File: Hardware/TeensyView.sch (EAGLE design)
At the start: 9 parts

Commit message: Proto 1 design complete
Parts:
- removed J3: (no value), SparkFun-Connectors:CONN_01
- added C1, C2, C3, C4: 1.0uF, SparkFun-Capacitors:1.0UF-0402-16V-10%
- added C5: 2.2uF, SparkFun-Capacitors:2.2UF-0805-25V-(+80/-20%)
- added C6: 4.7UF, SparkFun-Capacitors:4.7UF-1206-16V-(+80/-20%)
- added JP1, JP2, JP3: JUMPER-SMT_3_1-NC_TRACE_SILK, SparkFun-Jumpers:JUMPER-SMT_3_1-NC_TRACE_SILK
- added OLED1: OLED128X64SIDEREAR-MOUNT, TeensyViewDev:OLED128X64SIDEREAR-MOUNT
- added R1: 330k, SparkFun-Resistors:330KOHM-0603-1/10W-1%
- J1, J2: value (none) -> DNP; device SparkFun-Connectors:CONN_14 -> SparkFun-Connectors:CONN_14NO_SILK
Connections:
- new net !CS: JP1.2, OLED1.!CS!
- new net !RESET: J1.8, OLED1.!RESET!
- new net D/!C: J1.7, OLED1.D/!C!
- new net N$1: J1.12, JP1.3
- new net N$10: J2.1, JP3.3
- new net N$11: J2.7, JP3.1
- new net N$12: J1.13, JP2.3
- new net N$13: J2.6, JP2.1
- new net N$2: J1.11, JP1.1
- new net N$3: C4.2, OLED1.C1N
- new net N$4: C4.1, OLED1.C1P
- new net N$5: C3.2, OLED1.C2N
- new net N$6: C3.1, OLED1.C2P
- new net N$7: OLED1.IREF, R1.2
- new net N$8: C6.1, OLED1.VCOMH
- new net N$9: C5.1, OLED1.VCC
- new net SCLK: JP3.2, OLED1.SCLK
- new net SDIN: JP2.2, OLED1.SDIN
- new net VCC: C1.1, C2.1, J2.12, OLED1.VDD, OLED1.VDDB
- net GND: now also C1.2, C2.2, C5.2, C6.2, J1.1, OLED1.VSS, R1.1; no longer J3.1
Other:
- note added: "10"
- note added: "11"
- note added: "128x32 OLED on the Teensy 3 footprint."
- note added: "13"
- note added: "9"
- note added: "A4"
- note added: "A5"
- note added: "Connect directly to Teensy. Draws 30mA from the Teensy's 3.3v regulator."
- note added: "Teensy pin 0"
- note added: "Teensy pin 12"
- note added: "Teensy pin 13"
- note added: "Teensy pin 23"
- note added: "TeensyView"
- note added: "To use SPI: JP1: Select Chip Select. Choose (10 default) or 9. JP2: Select MOSI on pin 11 (default). JP3: Select SCLK on pin 13 (default). To use I2C: JP1: Drive logic high on pin 10 or 9. JP2: Select SDA0 on pin A4 JP3: Select SCL0 on pin A5"
- moved on the sheet: J1, J2

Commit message: Post review fixes
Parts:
- added JP4: JUMPER-SMT_3_2-NC_TRACE_SILK, SparkFun-Jumpers:JUMPER-SMT_3_2-NC_TRACE_SILK
- added R2, R3, R4: 4.7k, SparkFun-Resistors:4.7KOHM-0603-1/10W-1%
- C6: PROD_ID (none) -> CAP-10300
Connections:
- new net A4PU: JP4.3, R2.2
- new net A5PU: JP4.1, R3.2
- net !CS: now also R4.1
- net N$11: now also R3.1
- net N$13: now also R2.1
- net VCC: now also JP4.2, R4.2
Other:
- note added: "OLED Connections"
- note added: "Teensy Connections"
- note added: "To use SPI: JP1: Select Chip Select. Choose (10 default) or 9. JP2: Select MOSI on pin 11 (default). JP3: Select SCLK on pin 13 (default). To use I2C (Address: 0x7A): JP1: Drive logic high on pin 10 or 9. JP2: Select SDA0 on pin A4 JP3: Select SCL0 on pin A5"
- note removed: "To use SPI: JP1: Select Chip Select. Choose (10 default) or 9. JP2: Select MOSI on pin 11 (default). JP3: Select SCLK on pin 13 (default). To use I2C: JP1: Drive logic high on pin 10 or 9. JP2: Select SDA0 on pin A4 JP3: Select SCL0 on pin A5"
- moved on the sheet: J1, J2, JP1, JP2, JP3

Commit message: Going for proto 2
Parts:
- removed R2, R3: 4.7k, SparkFun-Resistors:4.7KOHM-0603-1/10W-1%
- added JP5: JUMPER-SMT_3_1-NC_TRACE_SILK, SparkFun-Jumpers:JUMPER-SMT_3_1-NC_TRACE_SILK
- JP4: value JUMPER-SMT_3_2-NC_TRACE_SILK -> JUMPER-SMT_3_1-NC_TRACE_SILK; device SparkFun-Jumpers:JUMPER-SMT_3_2-NC_TRACE_SILK -> SparkFun-Jumpers:JUMPER-SMT_3_1-NC_TRACE_SILK
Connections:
- removed net A4PU: JP4.3, R2.2
- removed net A5PU: JP4.1, R3.2
- new net N$14: J2.3, JP4.3
- new net N$15: J1.4, JP4.1
- new net N$16: J1.7, JP5.3
- new net N$17: J2.9, JP5.1
- net !RESET: now also JP4.2; no longer J1.8
- net D/!C: now also JP5.2; no longer J1.7
- net N$11: now also J2.2; no longer J2.7, R3.1
- net N$13: now also J1.9; no longer J2.6, R2.1
- net N$2: now also J2.8; no longer J1.11
- net VCC: no longer JP4.2
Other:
- note added: "14"
- note added: "15"
- note added: "2"
- note added: "20"
- note added: "21"
- note added: "5"
- note added: "7"
- note added: "Alternate( Audio Shield Compatible) D/!C!: 21 CS: 20 MOSI: 7 SCLK: 14 !RESET!: 2"
- note added: "Always connect power and ground as well."
- note added: "Connect directly to Teensy. Draws <1mA from the Teensy's 3.3v regulator. (1.6V to 4.0V tolerant)"
- note added: "Default (copper link side): D/!C!: 5 CS: 10 MOSI: 11 SCLK: 13 !RESET!: 15"
- note added: "User jumpers 1-5 to configure where the OLED's control lines are connected, then configure with code to match."
- note added: "v02"
- note removed: "9"
- note removed: "A5"
- note removed: "Connect directly to Teensy. Draws 30mA from the Teensy's 3.3v regulator."
- note removed: "To use SPI: JP1: Select Chip Select. Choose (10 default) or 9. JP2: Select MOSI on pin 11 (default). JP3: Select SCLK on pin 13 (default). To use I2C (Address: 0x7A): JP1: Drive logic high on pin 10 or 9. JP2: Select SDA0 on pin A4 JP3: Select SCL0 on pin A5"
- note removed: "v01"
- moved on the sheet: J1, J2, JP1, JP2, JP3, R4

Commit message: Moved silk.
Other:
- note added: "Connect directly to Teensy. Draws ~16mA from the Teensy's 3.3v regulator. (1.6V to 4.0V tolerant)"
- note removed: "Connect directly to Teensy. Draws <1mA from the Teensy's 3.3v regulator. (1.6V to 4.0V tolerant)"
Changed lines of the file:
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@@
 </text>
 <text x="5.08" y="175.26" size="5.08" layer="97" font="vector">TeensyView</text>
-<text x="10.16" y="167.64" size="1.778" layer="97" font="vector" align="top-left">Connect directly to Teensy.  Draws &lt;1mA from the
+<text x="10.16" y="167.64" size="1.778" layer="97" font="vector" align="top-left">Connect directly to Teensy.  Draws ~16mA from the
 Teensy's 3.3v regulator.
 (1.6V to 4.0V tolerant)</text>

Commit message: Applied Proto 2 review action items
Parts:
- R1: value 330k -> 820k; device SparkFun-Resistors:330KOHM-0603-1/10W-1% -> SparkFun-Resistors:820KOHM-0603-1/10W-1%
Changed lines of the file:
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@@
 <attribute name="PROD_ID" value="CAP-10300"/>
 </part>
-<part name="R1" library="SparkFun-Resistors" deviceset="330KOHM" device="-0603-1/10W-1%" value="330k"/>
+<part name="R1" library="SparkFun-Resistors" deviceset="820KOHM" device="-0603-1/10W-1%" value="820k"/>
 <part name="GND4" library="SparkFun-PowerSymbols" deviceset="GND" device=""/>
 <part name="GND5" library="SparkFun-PowerSymbols" deviceset="GND" device=""/>

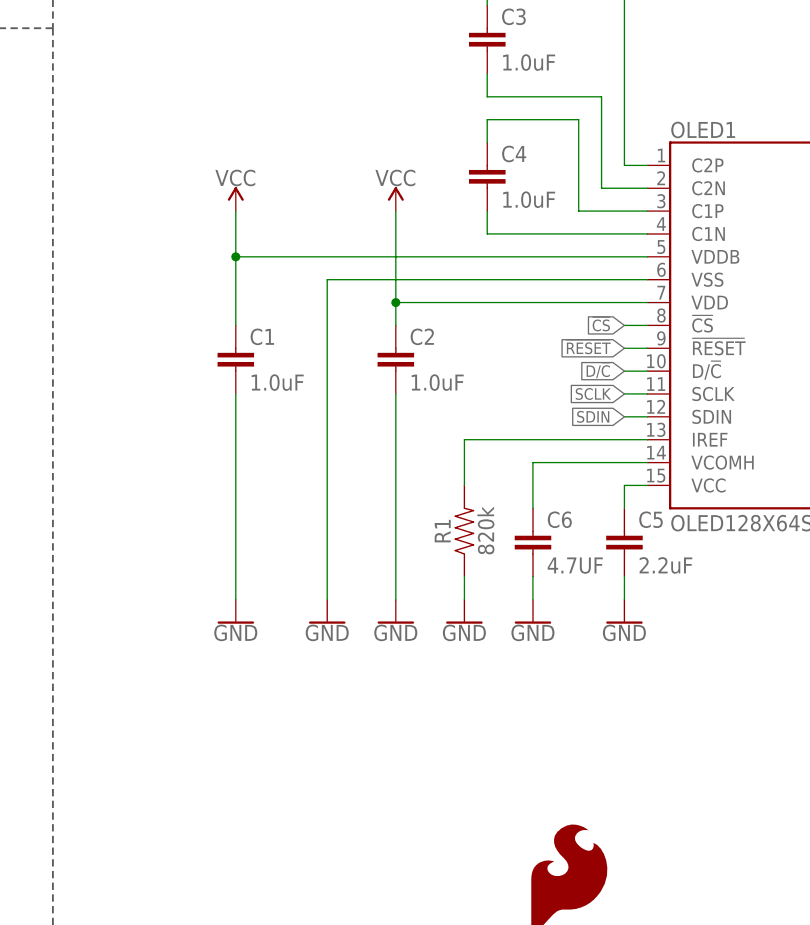
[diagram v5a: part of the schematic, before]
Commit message: Added TP to OLED's VCC
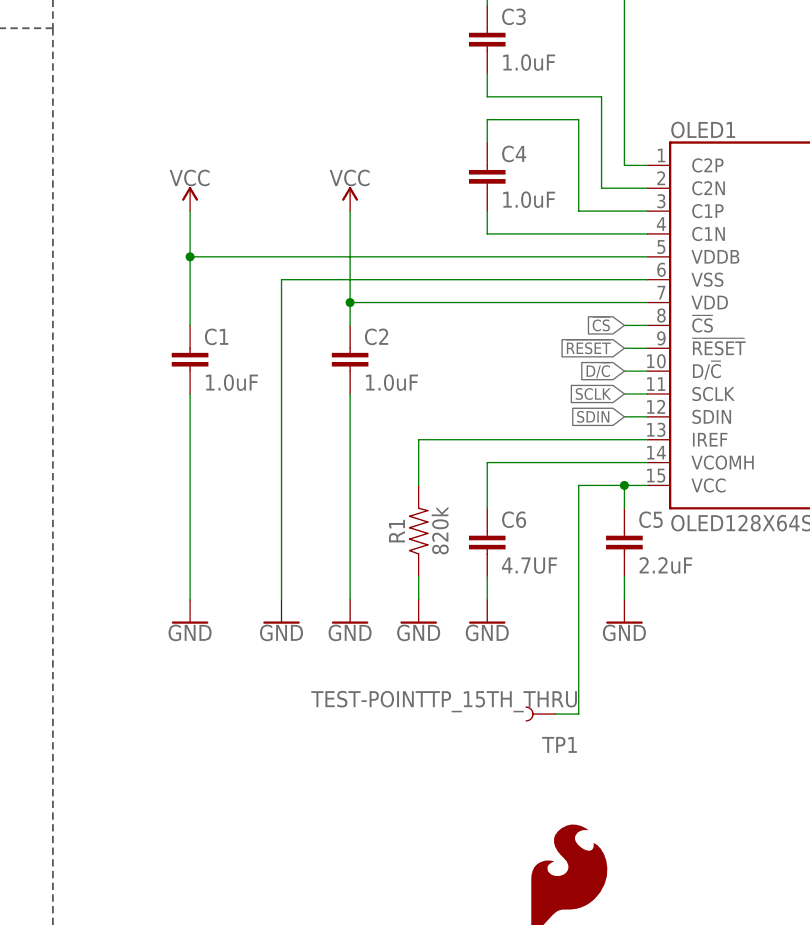
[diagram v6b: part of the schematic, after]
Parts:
- added TP1: TEST-POINTTP_15TH_THRU, SparkFun-Connectors:TEST-POINTTP_15TH_THRU
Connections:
- net N$9: now also TP1.1
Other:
- moved on the sheet: C1, C2, C6, R1
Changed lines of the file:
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@@
 <part name="JP4" library="SparkFun-Jumpers" deviceset="JUMPER-SMT_3_1-NC_TRACE" device="_SILK" value="JUMPER-SMT_3_1-NC_TRACE_SILK"/>
 <part name="JP5" library="SparkFun-Jumpers" deviceset="JUMPER-SMT_3_1-NC_TRACE" device="_SILK" value="JUMPER-SMT_3_1-NC_TRACE_SILK"/>
+<part name="TP1" library="SparkFun-Connectors" deviceset="TEST-POINT" device="TP_15TH_THRU" value="TEST-POINTTP_15TH_THRU"/>
 </parts>
 <sheets>
@@
 <instance part="LOGO3" gate="G$1" x="152.4" y="40.64"/>
 <instance part="OLED1" gate="G$1" x="213.36" y="121.92"/>
-<instance part="C1" gate="G$1" x="152.4" y="116.84"/>
-<instance part="C2" gate="G$1" x="170.18" y="116.84"/>
-<instance part="GND2" gate="1" x="170.18" y="88.9"/>
-<instance part="GND3" gate="1" x="152.4" y="88.9"/>
+<instance part="C1" gate="G$1" x="147.32" y="116.84"/>
+<instance part="C2" gate="G$1" x="165.1" y="116.84"/>
+<instance part="GND2" gate="1" x="165.1" y="88.9"/>
+<instance part="GND3" gate="1" x="147.32" y="88.9"/>
 <instance part="C3" gate="G$1" x="180.34" y="152.4"/>
 <instance part="C4" gate="G$1" x="180.34" y="137.16"/>
 <instance part="C5" gate="G$1" x="195.58" y="96.52"/>
-<instance part="C6" gate="G$1" x="185.42" y="96.52">
-<attribute name="PROD_ID" x="185.42" y="96.52" size="1.27" layer="96" display="off"/>
-</instance>
-<instance part="R1" gate="G$1" x="177.8" y="99.06" rot="R90"/>
+<instance part="C6" gate="G$1" x="180.34" y="96.52">
+<attribute name="PROD_ID" x="180.34" y="96.52" size="1.27" layer="96" display="off"/>
+</instance>
+<instance part="R1" gate="G$1" x="172.72" y="99.06" rot="R90"/>
 <instance part="GND4" gate="1" x="195.58" y="88.9"/>
-<instance part="GND5" gate="1" x="185.42" y="88.9"/>
-<instance part="GND6" gate="1" x="177.8" y="88.9"/>
-<instance part="GND7" gate="1" x="162.56" y="88.9"/>
+<instance part="GND5" gate="1" x="180.34" y="88.9"/>
+<instance part="GND6" gate="1" x="172.72" y="88.9"/>
+<instance part="GND7" gate="1" x="157.48" y="88.9"/>
 <instance part="GND8" gate="1" x="27.94" y="78.74" rot="MR0"/>
-<instance part="SUPPLY1" gate="G$1" x="152.4" y="134.62"/>
-<instance part="SUPPLY2" gate="G$1" x="170.18" y="134.62"/>
+<instance part="SUPPLY1" gate="G$1" x="147.32" y="134.62"/>
+<instance part="SUPPLY2" gate="G$1" x="165.1" y="134.62"/>
 <instance part="SUPPLY3" gate="G$1" x="106.68" y="91.44"/>
 <instance part="JP1" gate="G$1" x="78.74" y="63.5" smashed="yes" rot="MR90">
@@
 <attribute name="NAME" x="58.42" y="70.739" size="1.778" layer="95" font="vector" rot="MR180" align="top-left"/>
 </instance>
+<instance part="TP1" gate="G$1" x="187.96" y="78.74" rot="R180"/>
 </instances>
 <busses>
@@
 <pinref part="C2" gate="G$1" pin="2"/>
 <pinref part="GND2" gate="1" pin="GND"/>
-<wire x1="170.18" y1="114.3" x2="170.18" y2="91.44" width="0.1524" layer="91"/>
+<wire x1="165.1" y1="114.3" x2="165.1" y2="91.44" width="0.1524" layer="91"/>
 </segment>
 <segment>
 <pinref part="GND3" gate="1" pin="GND"/>
 <pinref part="C1" gate="G$1" pin="2"/>
-<wire x1="152.4" y1="91.44" x2="152.4" y2="114.3" width="0.1524" layer="91"/>
+<wire x1="147.32" y1="91.44" x2="147.32" y2="114.3" width="0.1524" layer="91"/>
 </segment>
 <segment>
@@
 <pinref part="GND5" gate="1" pin="GND"/>
 <pinref part="C6" gate="G$1" pin="2"/>
-<wire x1="185.42" y1="93.98" x2="185.42" y2="91.44" width="0.1524" layer="91"/>
+<wire x1="180.34" y1="93.98" x2="180.34" y2="91.44" width="0.1524" layer="91"/>
 </segment>
 <segment>
 <pinref part="GND6" gate="1" pin="GND"/>
 <pinref part="R1" gate="G$1" pin="1"/>
-<wire x1="177.8" y1="91.44" x2="177.8" y2="93.98" width="0.1524" layer="91"/>
+<wire x1="172.72" y1="91.44" x2="172.72" y2="93.98" width="0.1524" layer="91"/>
 </segment>
 <segment>
 <pinref part="OLED1" gate="G$1" pin="VSS"/>
 <pinref part="GND7" gate="1" pin="GND"/>
-<wire x1="198.12" y1="127" x2="162.56" y2="127" width="0.1524" layer="91"/>
-<wire x1="162.56" y1="127" x2="162.56" y2="91.44" width="0.1524" layer="91"/>
+<wire x1="198.12" y1="127" x2="157.48" y2="127" width="0.1524" layer="91"/>
+<wire x1="157.48" y1="127" x2="157.48" y2="91.44" width="0.1524" layer="91"/>
 </segment>
 <segment>
@@
 <pinref part="OLED1" gate="G$1" pin="IREF"/>
 <pinref part="R1" gate="G$1" pin="2"/>
-<wire x1="198.12" y1="109.22" x2="177.8" y2="109.22" width="0.1524" layer="91"/>
-<wire x1="177.8" y1="109.22" x2="177.8" y2="104.14" width="0.1524" layer="91"/>
+<wire x1="198.12" y1="109.22" x2="172.72" y2="109.22" width="0.1524" layer="91"/>
+<wire x1="172.72" y1="109.22" x2="172.72" y2="104.14" width="0.1524" layer="91"/>
 </segment>
 </net>
@@
 <pinref part="OLED1" gate="G$1" pin="VCOMH"/>
 <pinref part="C6" gate="G$1" pin="1"/>
-<wire x1="198.12" y1="106.68" x2="185.42" y2="106.68" width="0.1524" layer="91"/>
-<wire x1="185.42" y1="106.68" x2="185.42" y2="101.6" width="0.1524" layer="91"/>
+<wire x1="198.12" y1="106.68" x2="180.34" y2="106.68" width="0.1524" layer="91"/>
+<wire x1="180.34" y1="106.68" x2="180.34" y2="101.6" width="0.1524" layer="91"/>
 </segment>
 </net>
@@
 <wire x1="198.12" y1="104.14" x2="195.58" y2="104.14" width="0.1524" layer="91"/>
 <wire x1="195.58" y1="104.14" x2="195.58" y2="101.6" width="0.1524" layer="91"/>
+<wire x1="195.58" y1="104.14" x2="190.5" y2="104.14" width="0.1524" layer="91"/>
+<wire x1="190.5" y1="104.14" x2="190.5" y2="78.74" width="0.1524" layer="91"/>
+<pinref part="TP1" gate="G$1" pin="1"/>
+<wire x1="190.5" y1="78.74" x2="187.96" y2="78.74" width="0.1524" layer="91"/>
+<junction x="195.58" y="104.14"/>
 </segment>
 </net>
@@
 <pinref part="C1" gate="G$1" pin="1"/>
 <pinref part="OLED1" gate="G$1" pin="VDDB"/>
-<wire x1="152.4" y1="121.92" x2="152.4" y2="129.54" width="0.1524" layer="91"/>
-<wire x1="152.4" y1="129.54" x2="198.12" y2="129.54" width="0.1524" layer="91"/>
+<wire x1="147.32" y1="121.92" x2="147.32" y2="129.54" width="0.1524" layer="91"/>
+<wire x1="147.32" y1="129.54" x2="198.12" y2="129.54" width="0.1524" layer="91"/>
 <pinref part="SUPPLY1" gate="G$1" pin="VCC"/>
-<wire x1="152.4" y1="129.54" x2="152.4" y2="134.62" width="0.1524" layer="91"/>
-<junction x="152.4" y="129.54"/>
+<wire x1="147.32" y1="129.54" x2="147.32" y2="134.62" width="0.1524" layer="91"/>
+<junction x="147.32" y="129.54"/>
 </segment>
 <segment>
 <pinref part="OLED1" gate="G$1" pin="VDD"/>
 <pinref part="C2" gate="G$1" pin="1"/>
-<wire x1="198.12" y1="124.46" x2="170.18" y2="124.46" width="0.1524" layer="91"/>
-<wire x1="170.18" y1="124.46" x2="170.18" y2="121.92" width="0.1524" layer="91"/>
-<wire x1="170.18" y1="124.46" x2="170.18" y2="134.62" width="0.1524" layer="91"/>
+<wire x1="198.12" y1="124.46" x2="165.1" y2="124.46" width="0.1524" layer="91"/>
+<wire x1="165.1" y1="124.46" x2="165.1" y2="121.92" width="0.1524" layer="91"/>
+<wire x1="165.1" y1="124.46" x2="165.1" y2="134.62" width="0.1524" layer="91"/>
 <pinref part="SUPPLY2" gate="G$1" pin="VCC"/>
-<junction x="170.18" y="124.46"/>
-</segment>
-<segment>
+<junction x="165.1" y="124.46"/>
+</segment>
+<segment>

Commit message: worked through checklist and updated some parts, moved TP
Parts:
- C6: value 4.7UF -> 4.7uF
- OLED1: value OLED128X64SIDEREAR-MOUNT -> 32x128 OLED
- R1: value 820k -> 390k; device SparkFun-Resistors:820KOHM-0603-1/10W-1% -> SparkFun-Resistors:390KOHM-0603-1/10W-1%
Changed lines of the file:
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@@
 <part name="LOGO2" library="SparkFun-Aesthetics" deviceset="OSHW-LOGO" device="S"/>
 <part name="LOGO3" library="SparkFun-Aesthetics" deviceset="SFE_LOGO_NAME_FLAME" device=".1_INCH"/>
-<part name="OLED1" library="TeensyViewDev" deviceset="OLED128X64SIDE" device="REAR-MOUNT" value="OLED128X64SIDEREAR-MOUNT"/>
+<part name="OLED1" library="TeensyViewDev" deviceset="OLED128X64SIDE" device="REAR-MOUNT" value="32x128 OLED"/>
 <part name="C1" library="SparkFun-Capacitors" deviceset="1.0UF" device="-0402-16V-10%" value="1.0uF"/>
 <part name="C2" library="SparkFun-Capacitors" deviceset="1.0UF" device="-0402-16V-10%" value="1.0uF"/>
@@
 <part name="C4" library="SparkFun-Capacitors" deviceset="1.0UF" device="-0402-16V-10%" value="1.0uF"/>
 <part name="C5" library="SparkFun-Capacitors" deviceset="2.2UF" device="-0805-25V-(+80/-20%)" value="2.2uF"/>
-<part name="C6" library="SparkFun-Capacitors" deviceset="4.7UF" device="-1206-16V-(+80/-20%)" value="4.7UF">
+<part name="C6" library="SparkFun-Capacitors" deviceset="4.7UF" device="-1206-16V-(+80/-20%)" value="4.7uF">
 <attribute name="PROD_ID" value="CAP-10300"/>
 </part>
-<part name="R1" library="SparkFun-Resistors" deviceset="820KOHM" device="-0603-1/10W-1%" value="820k"/>
+<part name="R1" library="SparkFun-Resistors" deviceset="390KOHM" device="-0603-1/10W-1%" value="390k"/>
 <part name="GND4" library="SparkFun-PowerSymbols" deviceset="GND" device=""/>
 <part name="GND5" library="SparkFun-PowerSymbols" deviceset="GND" device=""/>
@@
 <instance part="LOGO2" gate="G$1" x="233.68" y="50.8"/>
 <instance part="LOGO3" gate="G$1" x="152.4" y="40.64"/>
-<instance part="OLED1" gate="G$1" x="213.36" y="121.92"/>
+<instance part="OLED1" gate="G$1" x="213.36" y="121.92" smashed="yes">
+<attribute name="NAME" x="200.66" y="142.748" size="1.778" layer="95" font="vector"/>
+<attribute name="VALUE" x="205.74" y="100.838" size="1.778" layer="96" font="vector" align="top-left"/>
+</instance>
 <instance part="C1" gate="G$1" x="147.32" y="116.84"/>
 <instance part="C2" gate="G$1" x="165.1" y="116.84"/>

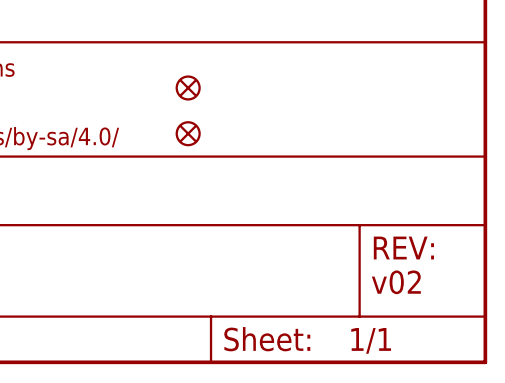
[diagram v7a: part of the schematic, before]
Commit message: Adjusted proto 2 in prep for reds review
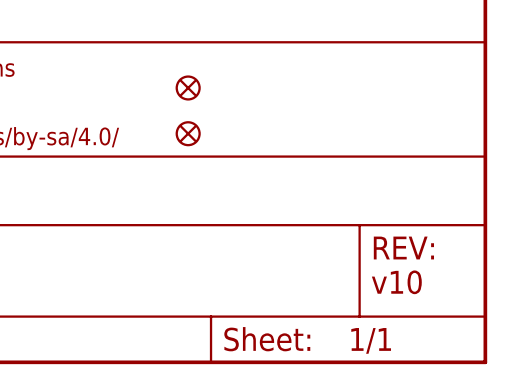
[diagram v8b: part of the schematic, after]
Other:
- note added: "v10"
- note removed: "v02"
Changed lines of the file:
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@@
 <?xml version="1.0" encoding="utf-8"?>
 <!DOCTYPE eagle SYSTEM "eagle.dtd">
-<eagle version="7.5.0">
+<eagle version="7.7.0">
 <drawing>
 <settings>
@@
 <sheet>
 <plain>
-<text x="236.22" y="7.62" size="2.54" layer="94" font="vector">v02</text>
+<text x="236.22" y="7.62" size="2.54" layer="94" font="vector">v10</text>
 <text x="149.86" y="7.62" size="2.54" layer="94" font="vector">Marshall Taylor</text>
 <wire x1="132.08" y1="185.42" x2="132.08" y2="154.94" width="0.2032" layer="97" style="longdash"/>
